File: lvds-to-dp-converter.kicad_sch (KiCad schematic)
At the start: 35 parts, among them U23 SN65DSI86ZXHR, U24 TLV73312PDBVT, U25 TLV73318PDBVT

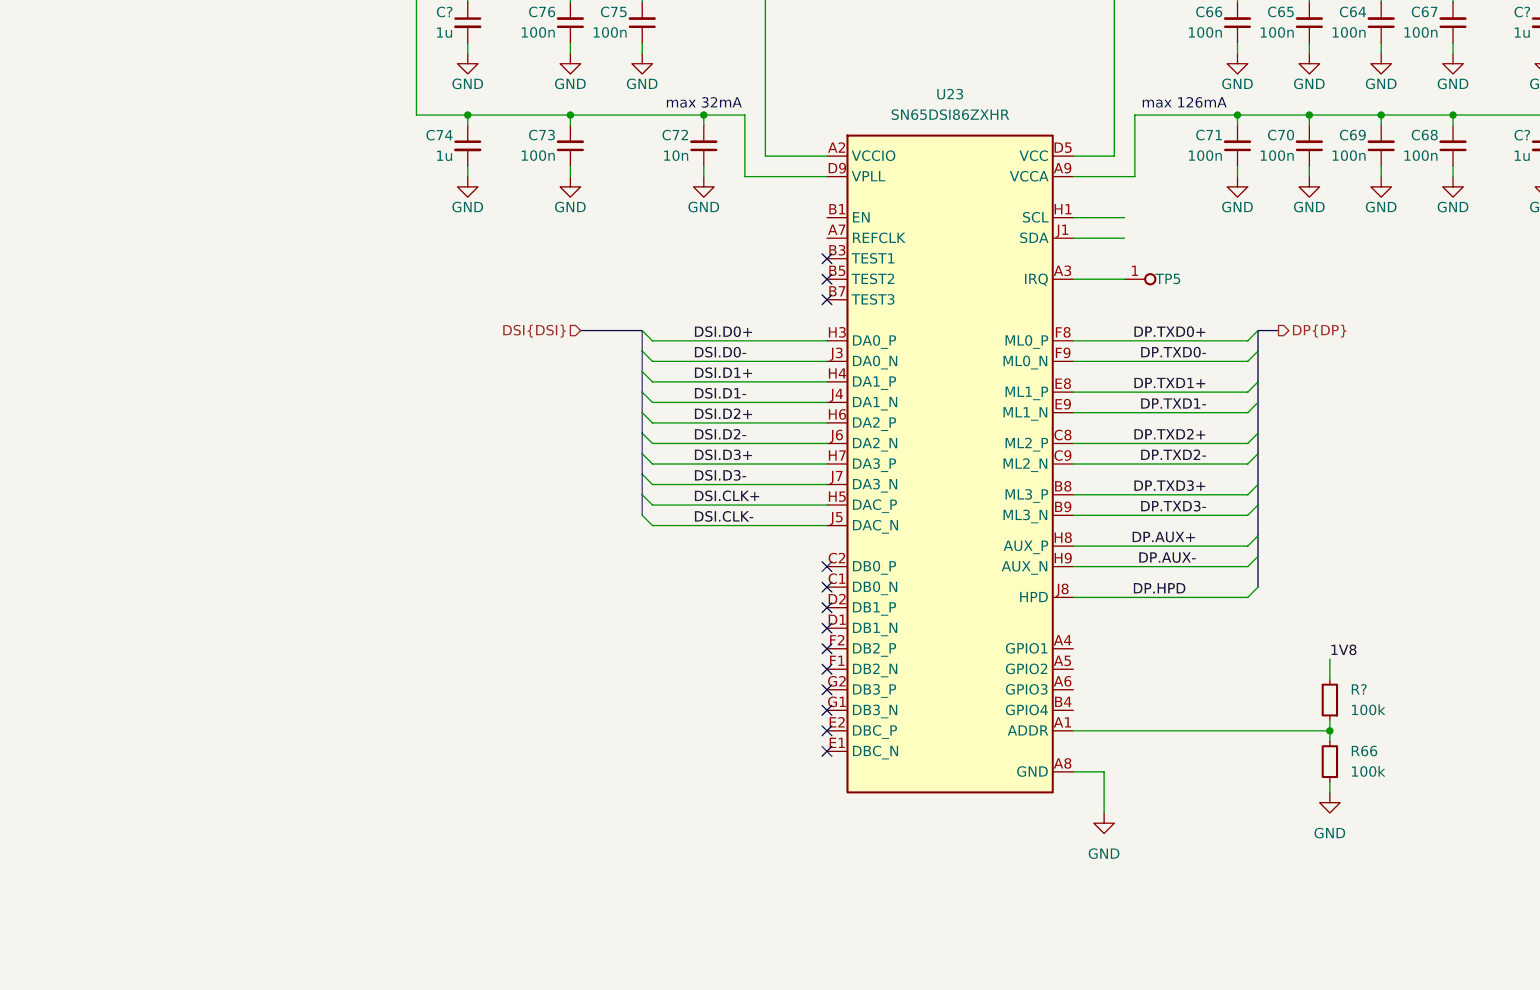
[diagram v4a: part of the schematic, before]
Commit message: [#82341] LVDS/DP Bridge: Add clock generator
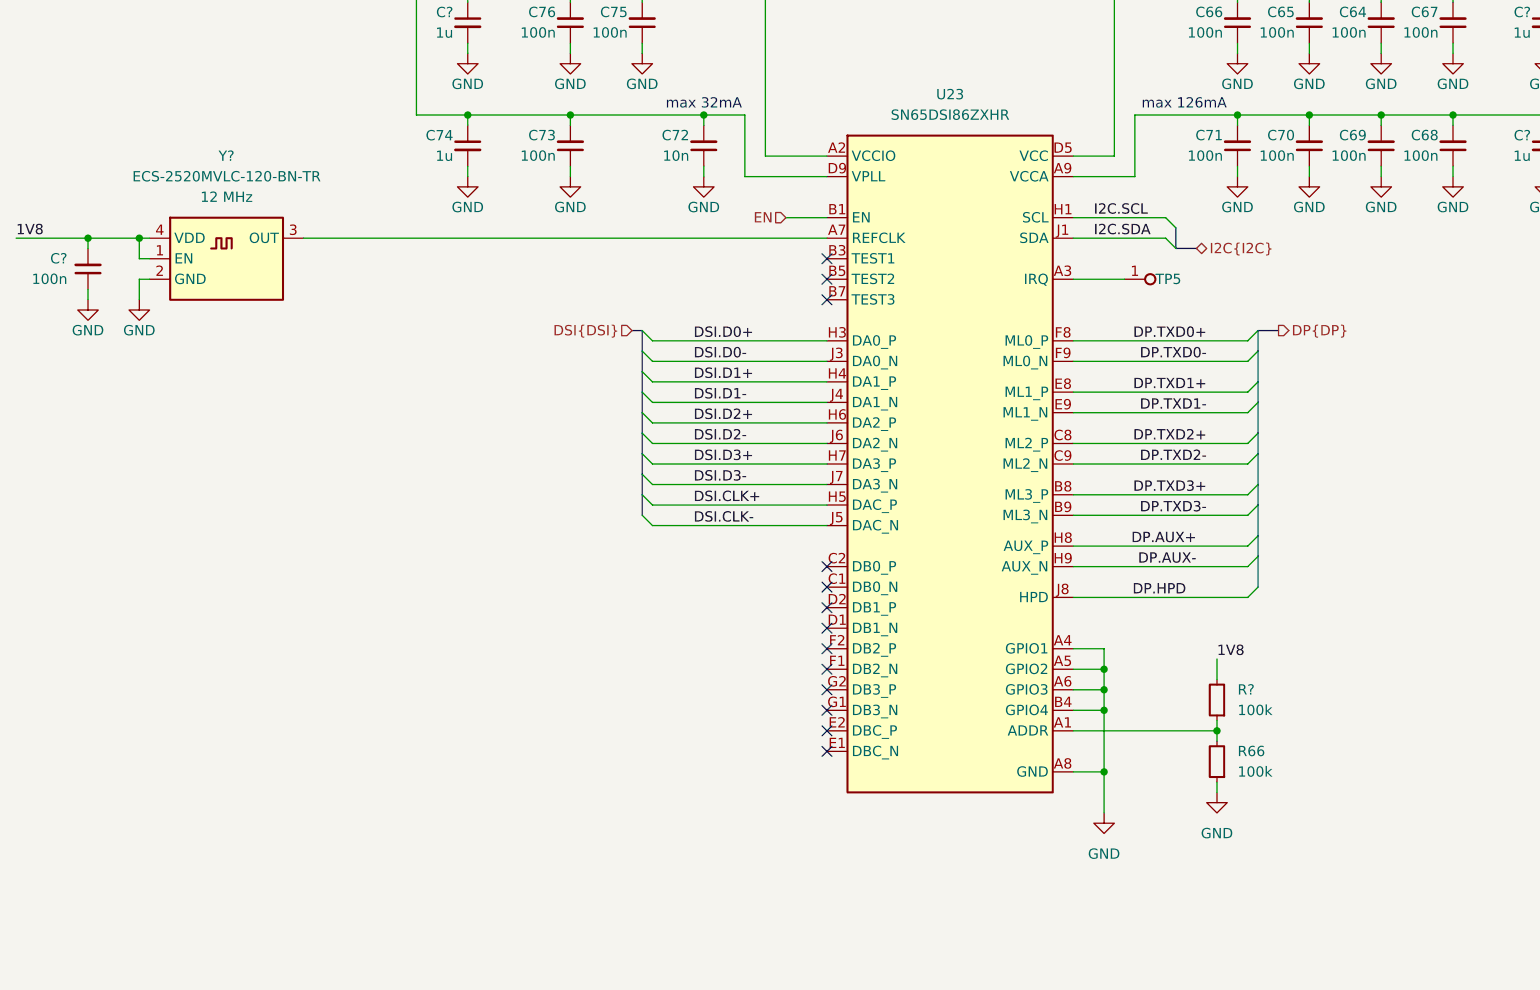
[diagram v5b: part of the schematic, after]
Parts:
- added C?: C_100n_0402, antmicro-footprints:C_0402_1005Metric, symbol Capacitors0402:C_100n_0402
- added Y?: Oscillator_12MHz_ESC_2520MV, antmicro-footprints:Oscillator_SMD_ECS_2520MV_2.5x2mm, symbol antmicroOscillators:Oscillator_12MHz_ESC_2520MV
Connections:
- net GND: now also U23.A4 (GPIO1), U23.A5 (GPIO2), U23.A6 (GPIO3), U23.B4 (GPIO4), C?.1, Y?.2 (GND)
- net VCCIO: now also C?.2, Y?.1 (EN), Y?.4 (VDD)
- net at U23.A7 (REFCLK): now also Y?.3 (OUT)
- net EN: now reaches U23.B1 (EN)
- net I2C.SCL: now reaches U23.H1 (SCL)
- net I2C.SDA: now reaches U23.J1 (SDA)
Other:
- moved on the sheet: R66, R?

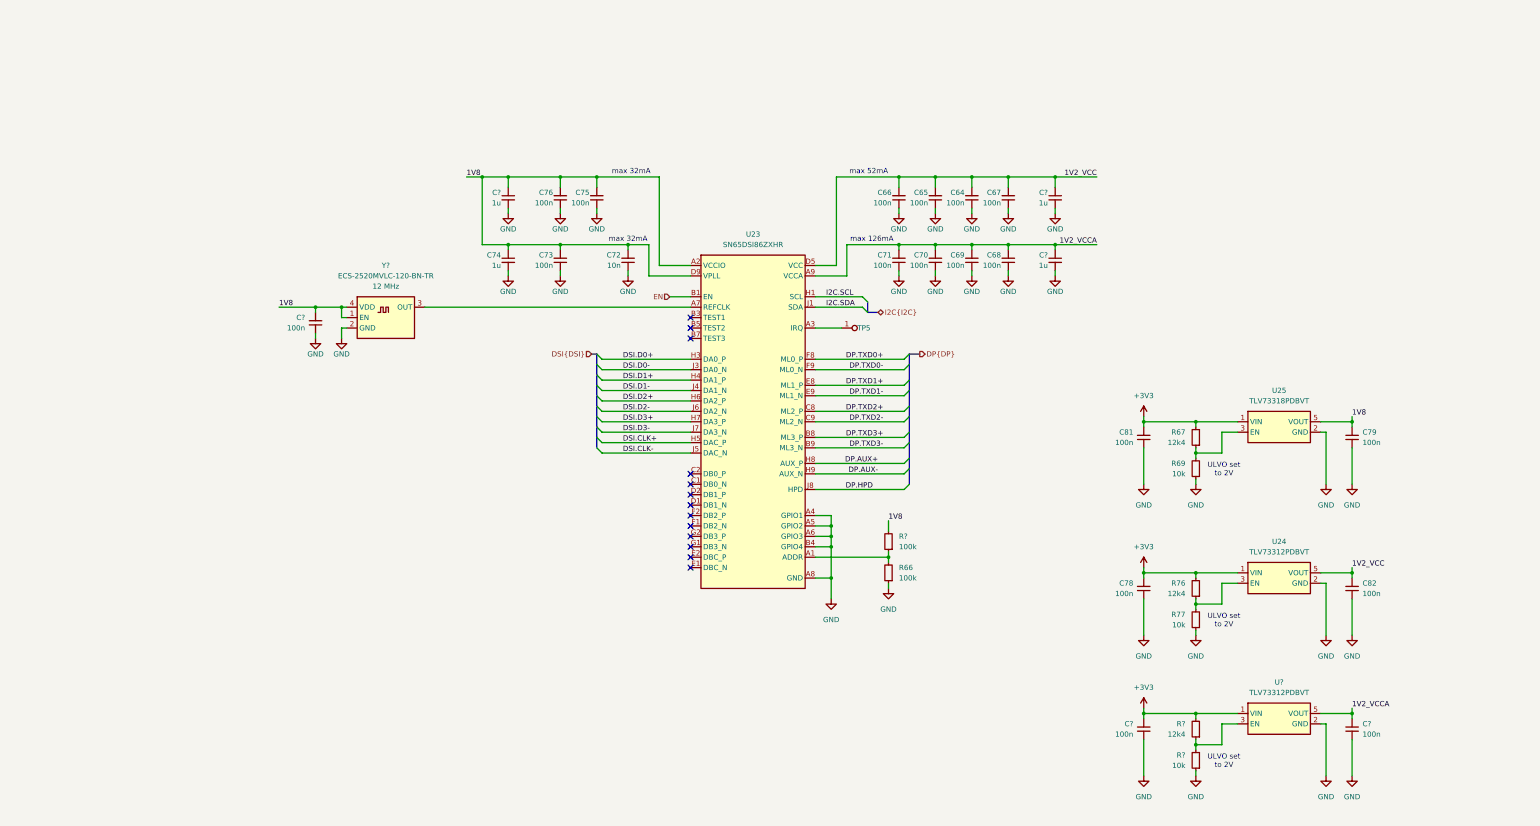
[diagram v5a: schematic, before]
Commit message: [#82341] LVDS/DP Bridge: Connect to OSM
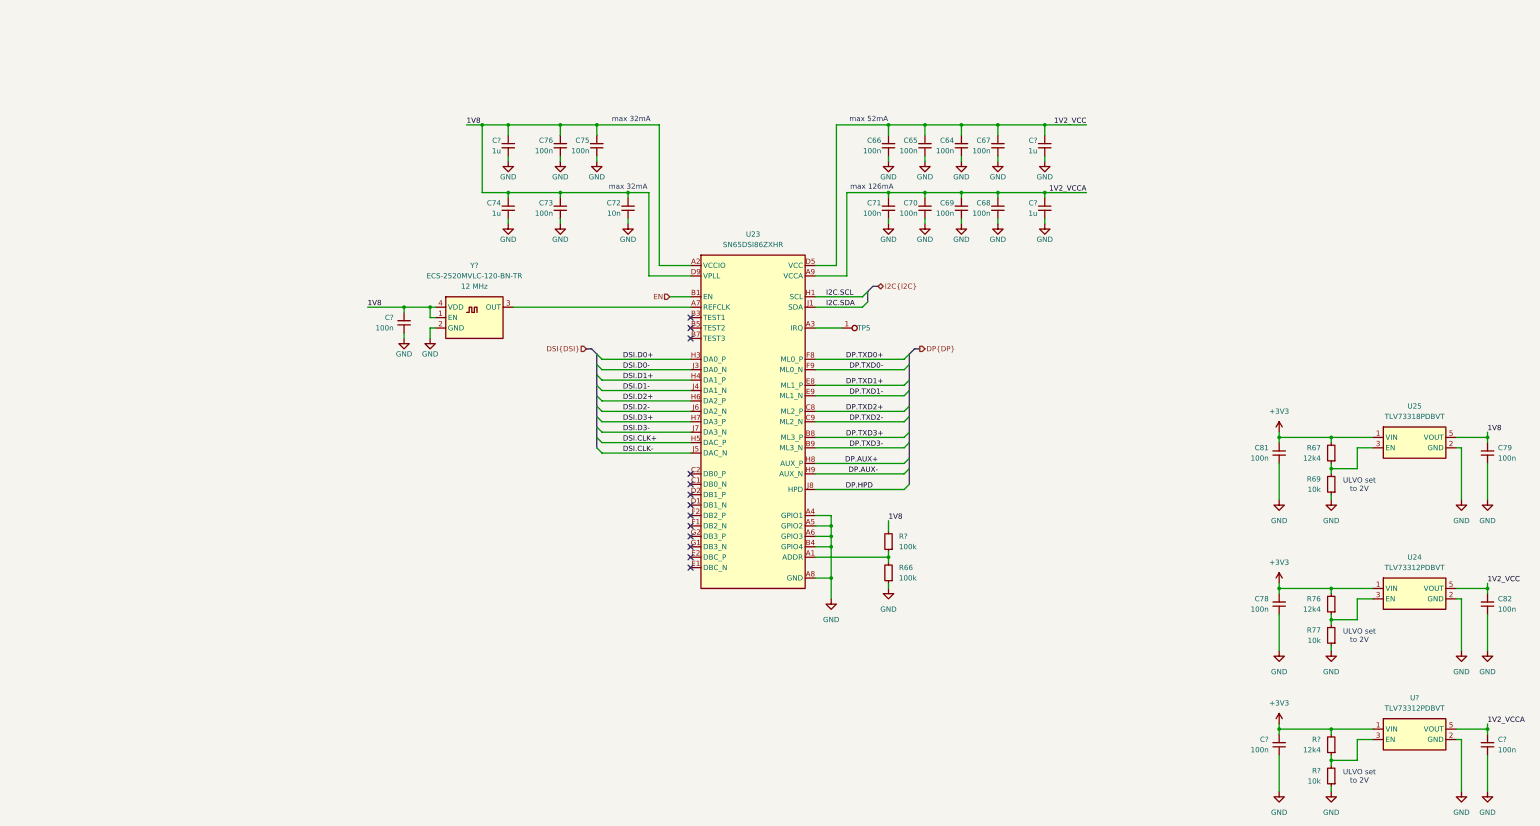
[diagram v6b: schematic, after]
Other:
- moved on the sheet: C64, C65, C66, C67, C68, C69, C70, C71, C72, C73, C74, C75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

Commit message: Annotate schematic
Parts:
- gave numbers to parts that had none: 11
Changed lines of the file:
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@@
 		(on_board yes)
 		(dnp no)
-		(property "Reference" "C?"
+		(property "Reference" "C86"
 			(at 373.38 218.4336 90)
 			(effects
@@
 			(project "bmc-reference-carrier-board"
 				(path "/5f636c45-3c15-4731-8931-4625e0dab7e4/8b9a8008-1846-45f3-9c02-8213595344f6"
-					(reference "C?")
+					(reference "C86")
 					(unit 1)
 				)
@@
 		(on_board yes)
 		(dnp no)
-		(property "Reference" "R?"
+		(property "Reference" "R78"
 			(at 227.33 168.91 90)
 			(effects
@@
 			(project "bmc-reference-carrier-board"
 				(path "/5f636c45-3c15-4731-8931-4625e0dab7e4/8b9a8008-1846-45f3-9c02-8213595344f6"
-					(reference "R?")
+					(reference "R78")
 					(unit 1)
 				)
@@
 		(dnp no)
 		(fields_autoplaced yes)
-		(property "Reference" "Y?"
+		(property "Reference" "Y3"
 			(at 123.825 102.87 0)
 			(effects
@@
 			(project ""
 				(path "/5f636c45-3c15-4731-8931-4625e0dab7e4/8b9a8008-1846-45f3-9c02-8213595344f6"
-					(reference "Y?")
+					(reference "Y3")
 					(unit 1)
 				)
@@
 		(on_board yes)
 		(dnp no)
-		(property "Reference" "C?"
+		(property "Reference" "C84"
 			(at 261.112 87.63 90)
 			(effects
@@
 			(project "bmc-reference-carrier-board"
 				(path "/5f636c45-3c15-4731-8931-4625e0dab7e4/8b9a8008-1846-45f3-9c02-8213595344f6"
-					(reference "C?")
+					(reference "C84")
 					(unit 1)
 				)
@@
 		(on_board yes)
 		(dnp no)
-		(property "Reference" "C?"
+		(property "Reference" "C83"
 			(at 261.112 72.39 90)
 			(effects
@@
 			(project "bmc-reference-carrier-board"
 				(path "/5f636c45-3c15-4731-8931-4625e0dab7e4/8b9a8008-1846-45f3-9c02-8213595344f6"
-					(reference "C?")
+					(reference "C83")
 					(unit 1)
 				)
@@
 		(on_board yes)
 		(dnp no)
-		(property "Reference" "C?"
+		(property "Reference" "C85"
 			(at 317.5 218.4336 90)
 			(effects
@@
 			(project "bmc-reference-carrier-board"
 				(path "/5f636c45-3c15-4731-8931-4625e0dab7e4/8b9a8008-1846-45f3-9c02-8213595344f6"
-					(reference "C?")
+					(reference "C85")
 					(unit 1)
 				)
@@
 		(dnp no)
 		(fields_autoplaced yes)
-		(property "Reference" "U?"
+		(property "Reference" "U26"
 			(at 353.06 208.28 0)
 			(effects
@@
 			(project "bmc-reference-carrier-board"
 				(path "/5f636c45-3c15-4731-8931-4625e0dab7e4/8b9a8008-1846-45f3-9c02-8213595344f6"
-					(reference "U?")
+					(reference "U26")
 					(unit 1)
 				)
@@
 		(on_board yes)
 		(dnp no)
-		(property "Reference" "C?"
+		(property "Reference" "C80"
 			(at 130.302 72.39 90)
 			(effects
@@
 			(project "bmc-reference-carrier-board"
 				(path "/5f636c45-3c15-4731-8931-4625e0dab7e4/8b9a8008-1846-45f3-9c02-8213595344f6"
-					(reference "C?")
+					(reference "C80")
 					(unit 1)
 				)
@@
 		(on_board yes)
 		(dnp no)
-		(property "Reference" "R?"
+		(property "Reference" "R79"
 			(at 330.2 218.44 90)
 			(effects
@@
 			(project "bmc-reference-carrier-board"
 				(path "/5f636c45-3c15-4731-8931-4625e0dab7e4/8b9a8008-1846-45f3-9c02-8213595344f6"
-					(reference "R?")
+					(reference "R79")
 					(unit 1)
 				)
@@
 		(on_board yes)
 		(dnp no)
-		(property "Reference" "C?"
+		(property "Reference" "C77"
 			(at 104.14 115.5636 90)
 			(effects
@@
 			(project "bmc-reference-carrier-board"
 				(path "/5f636c45-3c15-4731-8931-4625e0dab7e4/8b9a8008-1846-45f3-9c02-8213595344f6"
-					(reference "C?")
+					(reference "C77")
 					(unit 1)
 				)
@@
 		(on_board yes)
 		(dnp no)
-		(property "Reference" "R?"
+		(property "Reference" "R80"
 			(at 330.2 226.06 90)
 			(effects
@@
 			(project "bmc-reference-carrier-board"
 				(path "/5f636c45-3c15-4731-8931-4625e0dab7e4/8b9a8008-1846-45f3-9c02-8213595344f6"
-					(reference "R?")
+					(reference "R80")
 					(unit 1)
 				)
